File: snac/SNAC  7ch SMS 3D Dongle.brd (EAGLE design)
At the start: 37.3 x 23.8 mm, 14 parts, among them IC1 MAX660CPACS, IC2 4030D, K2 692112030100, Q9 BC849SMD, X2 STEREOJACK

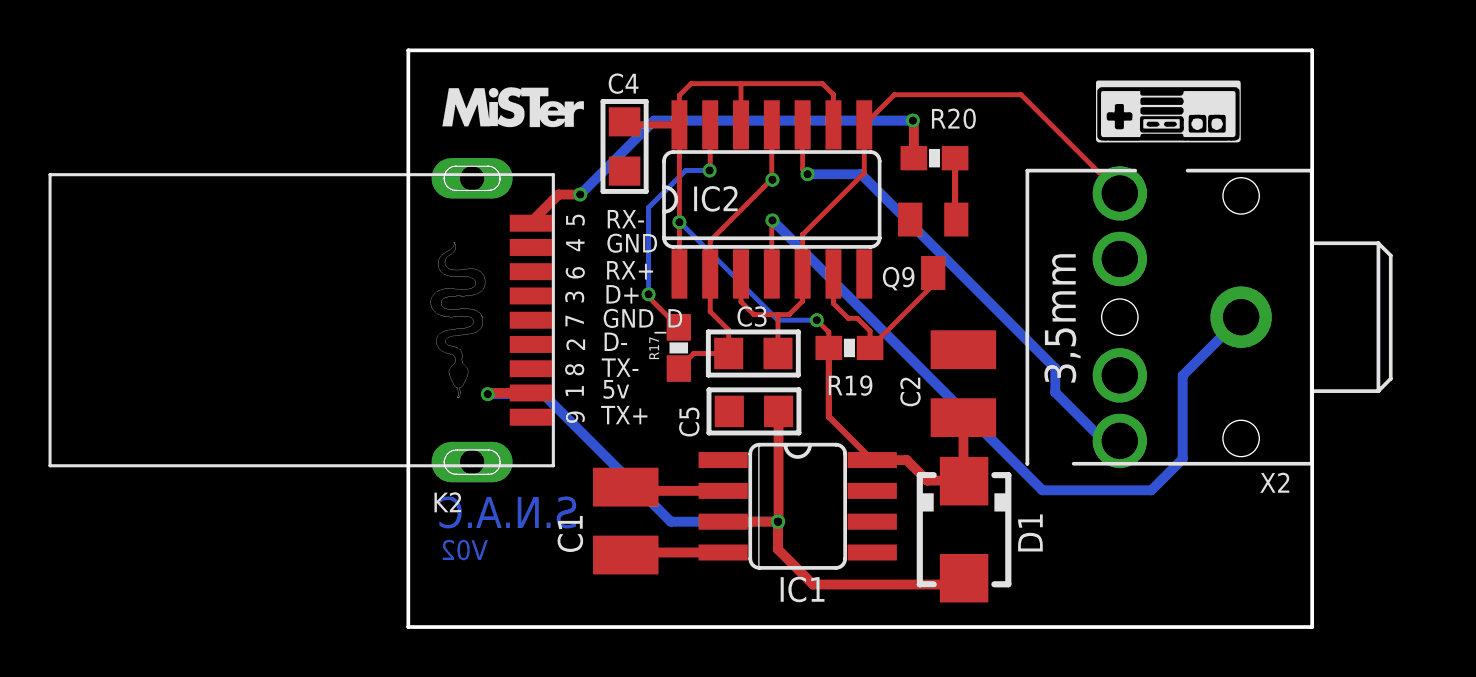
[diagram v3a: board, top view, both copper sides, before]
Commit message: XOR Osc on 3D boards needed an extra resistor
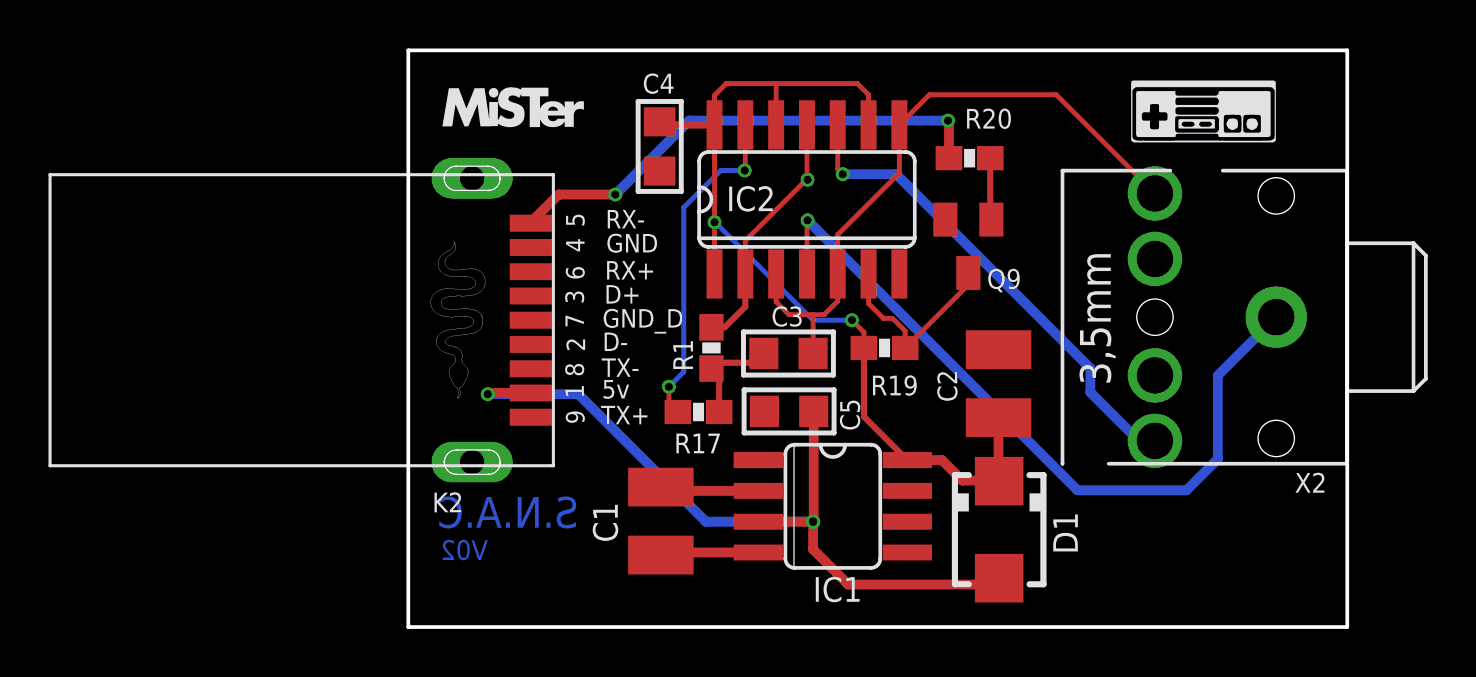
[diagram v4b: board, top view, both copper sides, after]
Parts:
- added R1: 10K, SparkFun:0603-RES
- C3: value 10nF -> 47nF
- moved R17 2.76 mm to (13.3, 10.2), turned to 0 degrees
- moved C1 1.45 mm to (11.7, 5.66)
- moved D1 1.45 mm to (25.7, 5.31)
- moved IC1 1.45 mm to (18.8, 6.27)
- moved Q9 1.45 mm to (24.4, 17.0)
- moved R19 1.45 mm to (20.9, 12.8)
- moved R20 1.45 mm to (24.4, 20.6)
- moved X2 1.45 mm to (39.8, 14.0)
- moved C3 1.45 mm to (17.0, 12.6)
- moved C4 1.45 mm to (11.7, 21.1)
- moved C5 1.45 mm to (17.0, 10.2)
- moved C2 1.45 mm to (25.6, 11.3)
- moved IC2 1.45 mm to (17.7, 18.9)
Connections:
- new net N$6: IC2.11, IC2.2, R1.2
- net N$5: now also R1.1; no longer IC2.11, IC2.2
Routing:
- net N$6: track 0.00 -> 10.4 mm, vias 0 -> 1
- net N$5: track 13.2 -> 4.34 mm, vias 1 -> 0
- net N$10: track 10.5 -> 13.9 mm
- net HV: track 32.3 -> 33.8 mm
- net LV6: track 19.1 -> 20.5 mm
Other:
- board size 37.3 x 23.8 mm -> 38.7 x 23.8 mm
